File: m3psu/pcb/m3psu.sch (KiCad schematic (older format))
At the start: 0 parts

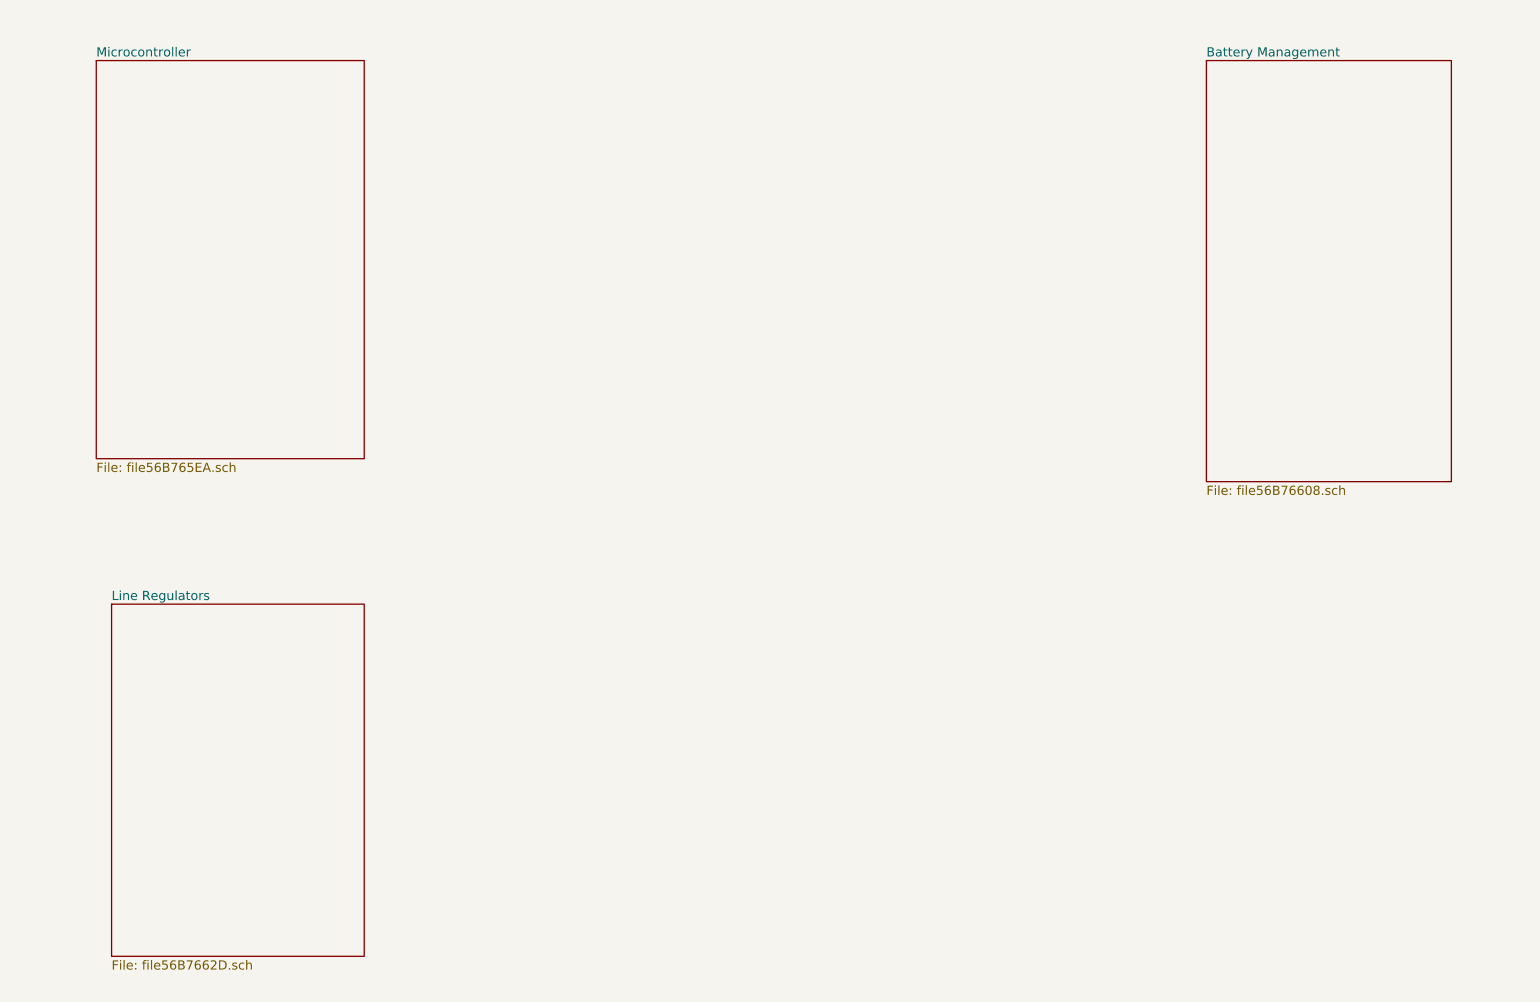
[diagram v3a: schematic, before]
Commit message: Added current monitor and control for pyros. Modified DC/DC converters.
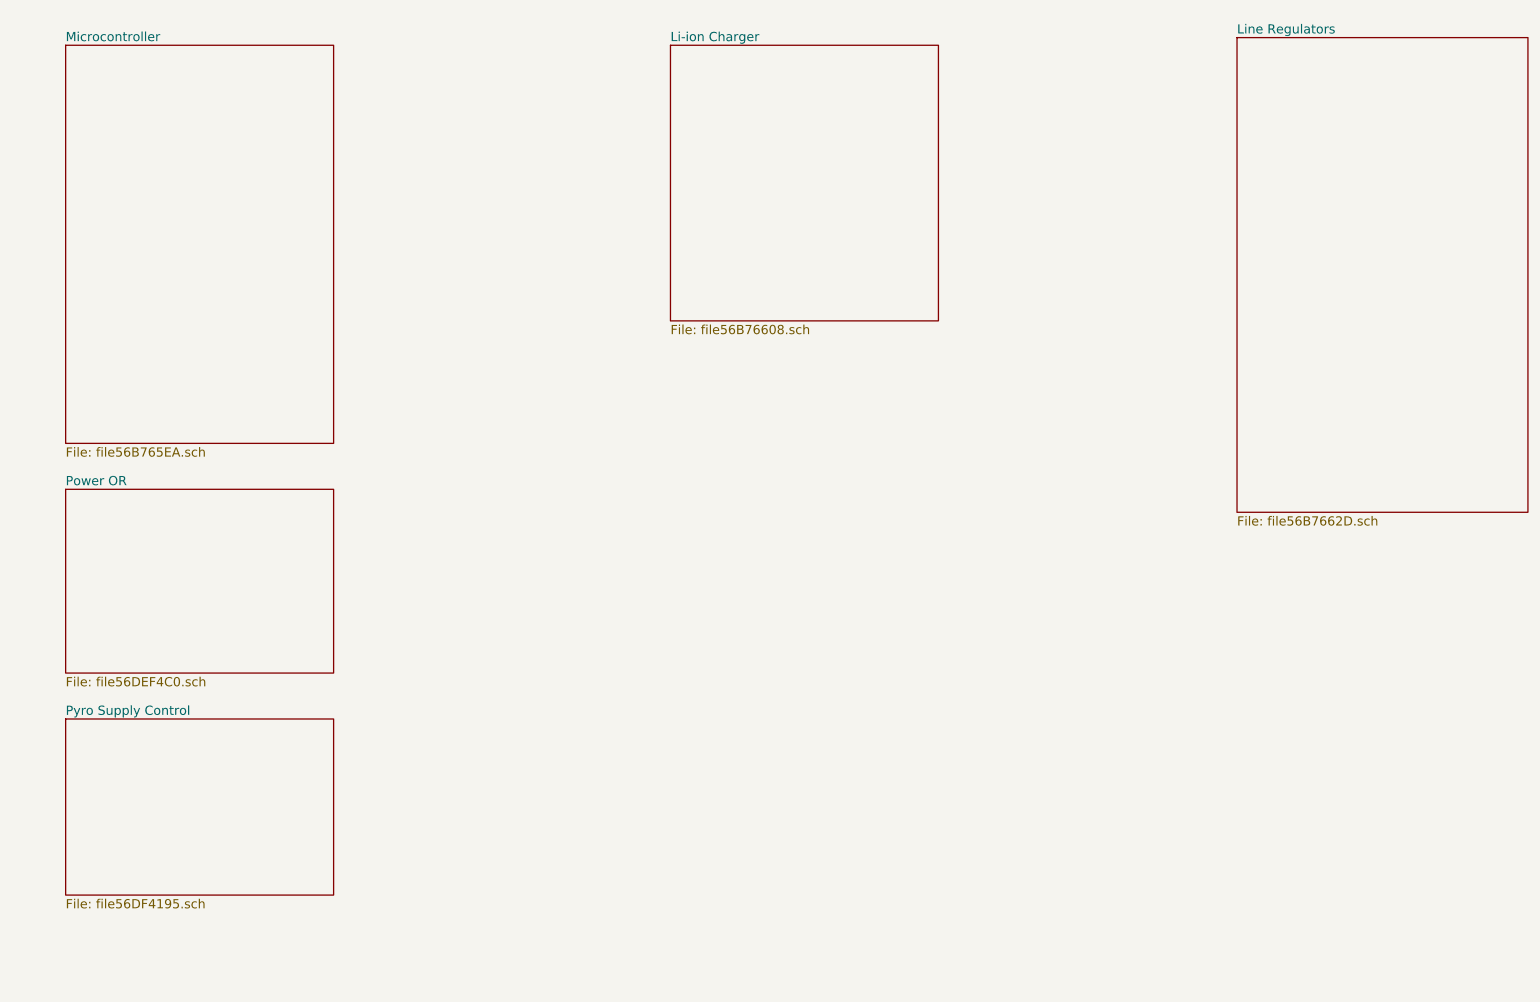
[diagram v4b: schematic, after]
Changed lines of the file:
@@
 $Descr A4 11693 8268
 encoding utf-8
-Sheet 1 10
+Sheet 1 12
 Title ""
 Date ""
@@
 $EndDescr
 $Sheet
-S 1400 1000 1750 2600
+S 1200 900  1750 2600
 U 56B765EB
 F0 "Microcontroller" 60
@@
 $EndSheet
 $Sheet
-S 8650 1000 1600 2750
+S 5150 900  1750 1800
 U 56B76609
-F0 "Battery Management" 60
+F0 "Li-ion Charger" 60
 F1 "file56B76608.sch" 60
 $EndSheet
 $Sheet
-S 1500 4550 1650 2300
+S 8850 850  1900 3100
 U 56B7662E
 F0 "Line Regulators" 60
 F1 "file56B7662D.sch" 60
 $EndSheet
+$Sheet
+S 1200 3800 1750 1200
+U 56DEF4C1
+F0 "Power OR" 60
+F1 "file56DEF4C0.sch" 60
+$EndSheet
+$Sheet
+S 1200 5300 1750 1150
+U 56DF4196
+F0 "Pyro Supply Control" 60
+F1 "file56DF4195.sch" 60
+$EndSheet
 $EndSCHEMATC

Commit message: Changes in arrangement of schematic. Started wiring interconnects. WIP.
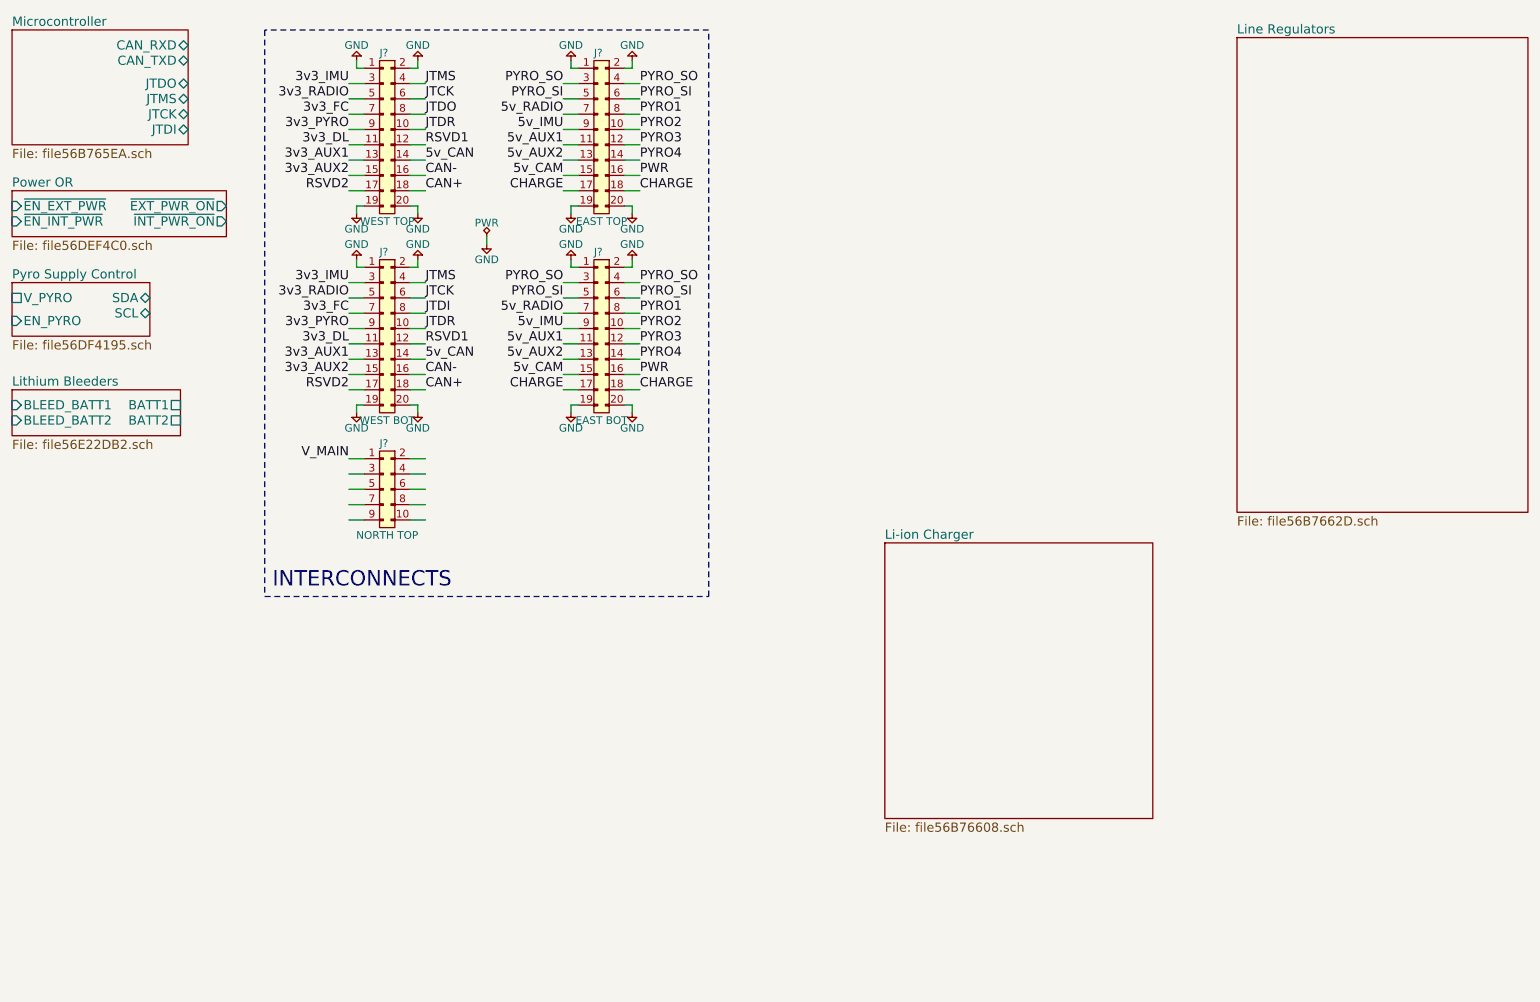
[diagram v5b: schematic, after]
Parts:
- added J?: WEST TOP, symbol CONN_02x10
- added J?: EAST TOP, symbol CONN_02x10
- added J?: WEST BOT, symbol CONN_02x10
- added J?: EAST BOT, symbol CONN_02x10
- added J?: NORTH TOP, symbol CONN_02x05
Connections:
- net labels added: 3v3_AUX1, 3v3_AUX2, 3v3_DL, 3v3_FC, 3v3_IMU, 3v3_PYRO, 3v3_RADIO, 5v_AUX1, 5v_AUX2, 5v_CAM, 5v_CAN, 5v_IMU, 5v_RADIO, CAN+, CAN-, CHARGE, GND, JTCK, JTDI, JTDO, JTDR, JTMS, PWR, PYRO1, PYRO2, PYRO3, PYRO4, PYRO_SI, PYRO_SO, RSVD1, RSVD2, V_MAIN
- wire segments 0 -> 107
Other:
- note added: "INTERCONNECTS"

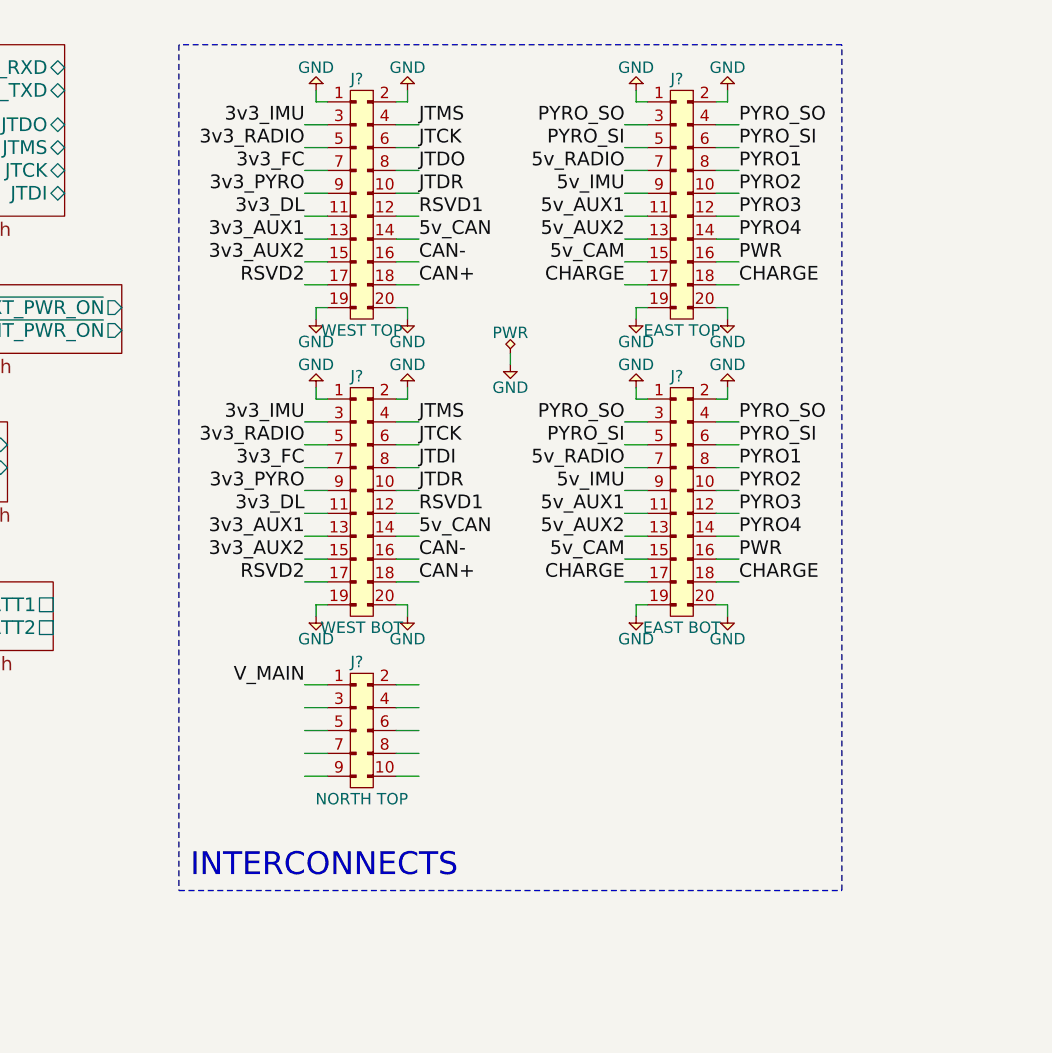
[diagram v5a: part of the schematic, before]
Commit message: Changes to Li-ion charger, north local interconnect.
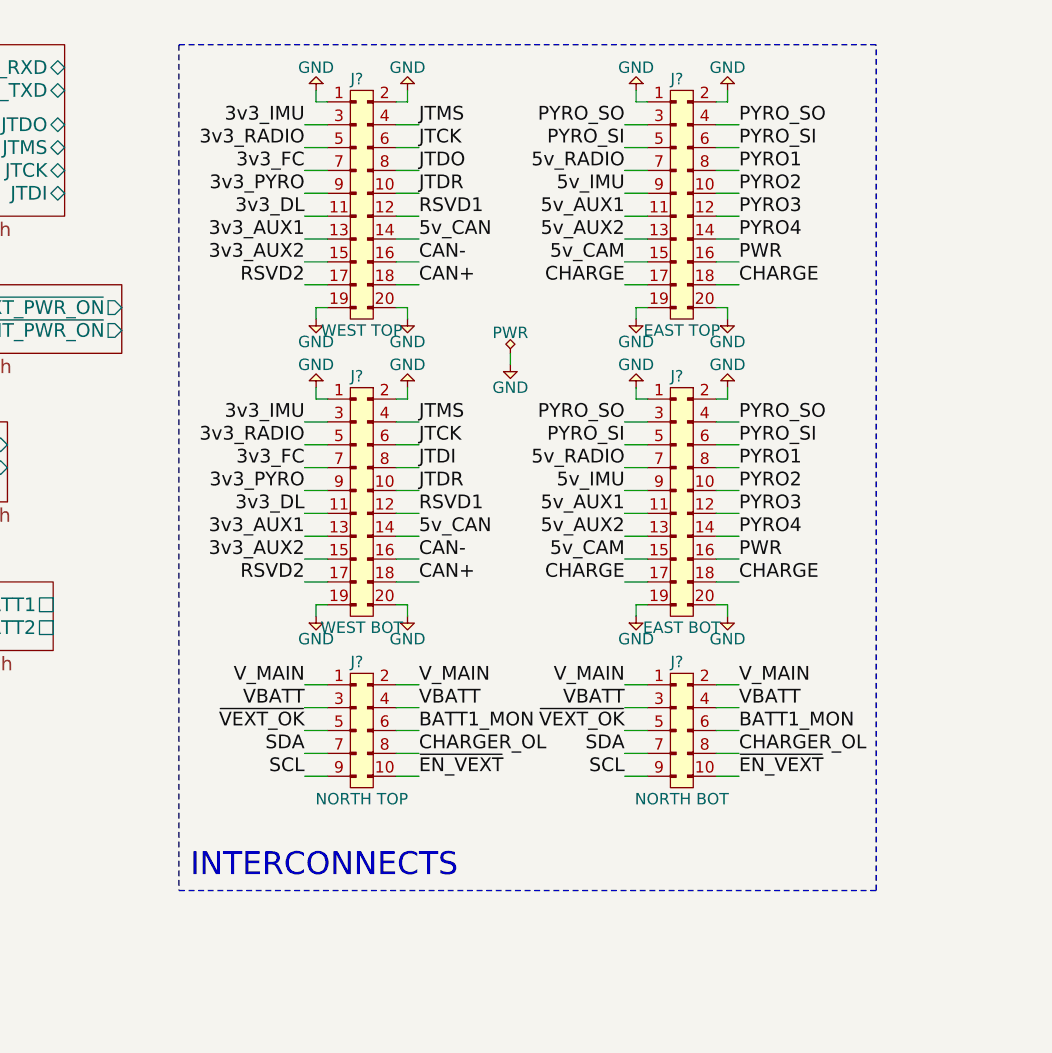
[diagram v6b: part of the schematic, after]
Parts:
- added J?: NORTH BOT, symbol CONN_02x05
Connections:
- net labels added: BATT1_MON, CHARGER_OL, SCL, SDA, VBATT, ~EN_VEXT, ~VEXT_OK
- wire segments 107 -> 117
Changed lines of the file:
@@
 	4850 2450 4950 2450
 Wire Notes Line
-	5400 800  2500 800
+	5550 800  2500 800
 Wire Notes Line
-	2500 4500 5400 4500
+	2500 4500 5550 4500
 Wire Notes Line
-	5400 4500 5400 800
+	5550 4500 5550 800
 Wire Notes Line
 	2500 800  2500 4500
@@
 Wire Wire Line
 	3450 3900 3550 3900
-Wire Wire Line
-	3450 4000 3550 4000
 Text Label 3050 3600 2    60   ~ 0
 V_MAIN
@@
 F5 "BLEED_BATT2" I L 850 3350 60
 $EndSheet
+Text Label 3550 3600 0    60   ~ 0
+V_MAIN
+Text Label 3050 3900 2    60   ~ 0
+SDA
+Text Label 3050 4000 2    60   ~ 0
+SCL
+Text Label 3050 3700 2    60   ~ 0
+VBATT
+Text Label 3550 3800 0    60   ~ 0
+BATT1_MON
+Text Label 3550 3700 0    60   ~ 0
+VBATT
+Text Label 3050 3800 2    60   ~ 0
+~VEXT_OK
+Text Label 3550 3900 0    60   ~ 0
+CHARGER_OL
+Wire Wire Line
+	3450 4000 3550 4000
+Text Label 3550 4000 0    60   ~ 0
+~EN_VEXT
+$Comp
+L CONN_02x05 J?
+U 1 1 56E6948A
+P 4750 3600
+F 0 "J?" H 4650 3700 50  0000 L CNN
+F 1 "NORTH BOT" H 4700 3100 50  0000 C CNN
+F 2 "" H 4750 3600 50  0001 C CNN
+F 3 "" H 4750 3600 50  0001 C CNN
+	1    4750 3600
+	1    0    0    -1
+$EndComp
+Wire Wire Line
+	4550 3600 4450 3600
+Wire Wire Line
+	4550 3700 4450 3700
+Wire Wire Line
+	4550 3800 4450 3800
+Wire Wire Line
+	4550 3900 4450 3900
+Wire Wire Line
+	4550 4000 4450 4000
+Wire Wire Line
+	4850 3600 4950 3600
+Wire Wire Line
+	4850 3700 4950 3700
+Wire Wire Line
+	4850 3800 4950 3800
+Wire Wire Line
+	4850 3900 4950 3900
+Text Label 4450 3600 2    60   ~ 0
+V_MAIN
+Text Label 4950 3600 0    60   ~ 0
+V_MAIN
+Text Label 4450 3900 2    60   ~ 0
+SDA
+Text Label 4450 4000 2    60   ~ 0
+SCL
+Text Label 4450 3700 2    60   ~ 0
+VBATT
+Text Label 4950 3800 0    60   ~ 0
+BATT1_MON
+Text Label 4950 3700 0    60   ~ 0
+VBATT
+Text Label 4450 3800 2    60   ~ 0
+~VEXT_OK
+Text Label 4950 3900 0    60   ~ 0
+CHARGER_OL
+Wire Wire Line
+	4850 4000 4950 4000
+Text Label 4950 4000 0    60   ~ 0
+~EN_VEXT
 $EndSCHEMATC
